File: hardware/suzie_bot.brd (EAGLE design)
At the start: 98.7 x 71.1 mm, 20 parts, among them IC1 LT1529CT33, IC2 L9637DDIP-ADAPTED, Y1 1.8432, Y2 6.0

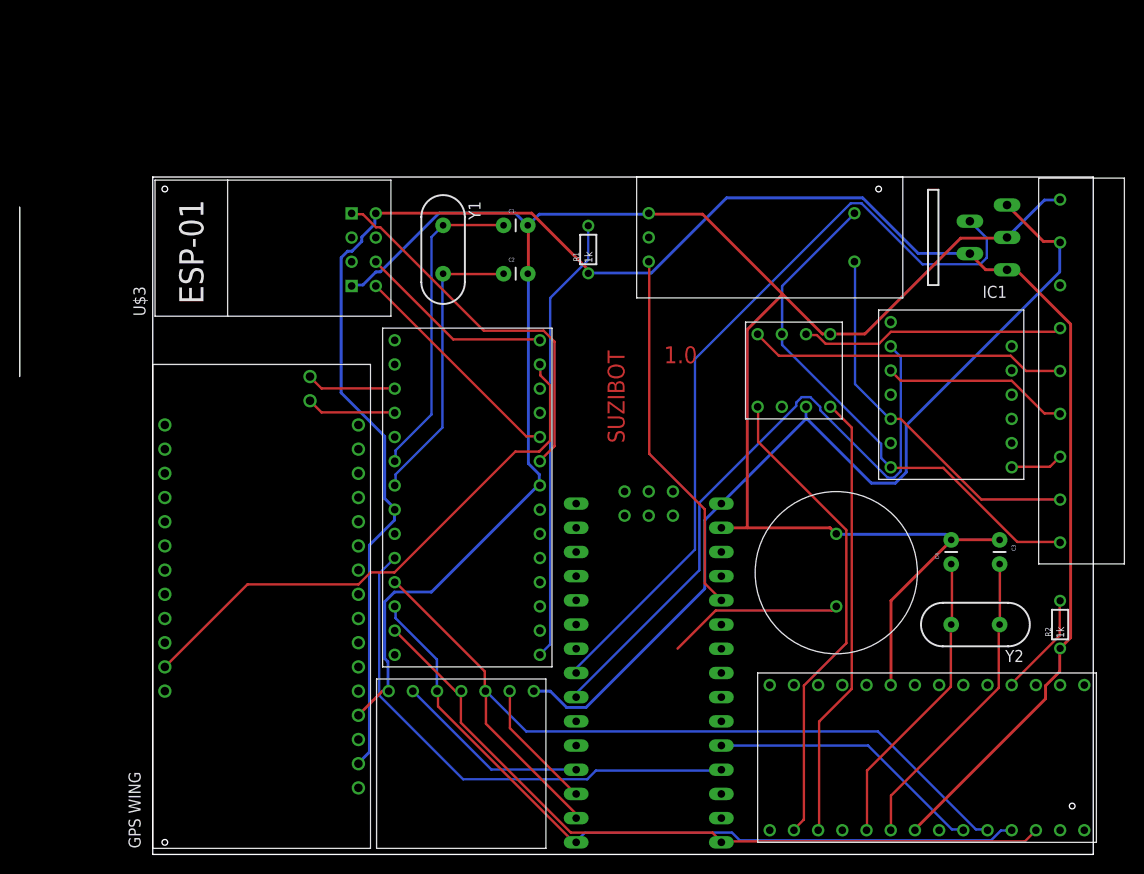
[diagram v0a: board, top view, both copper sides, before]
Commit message: Totally working. IT WAS VOLTAGE LEVELS AND CRYSTAL CAPACITANCE PROBLEMS ALL ALONG.
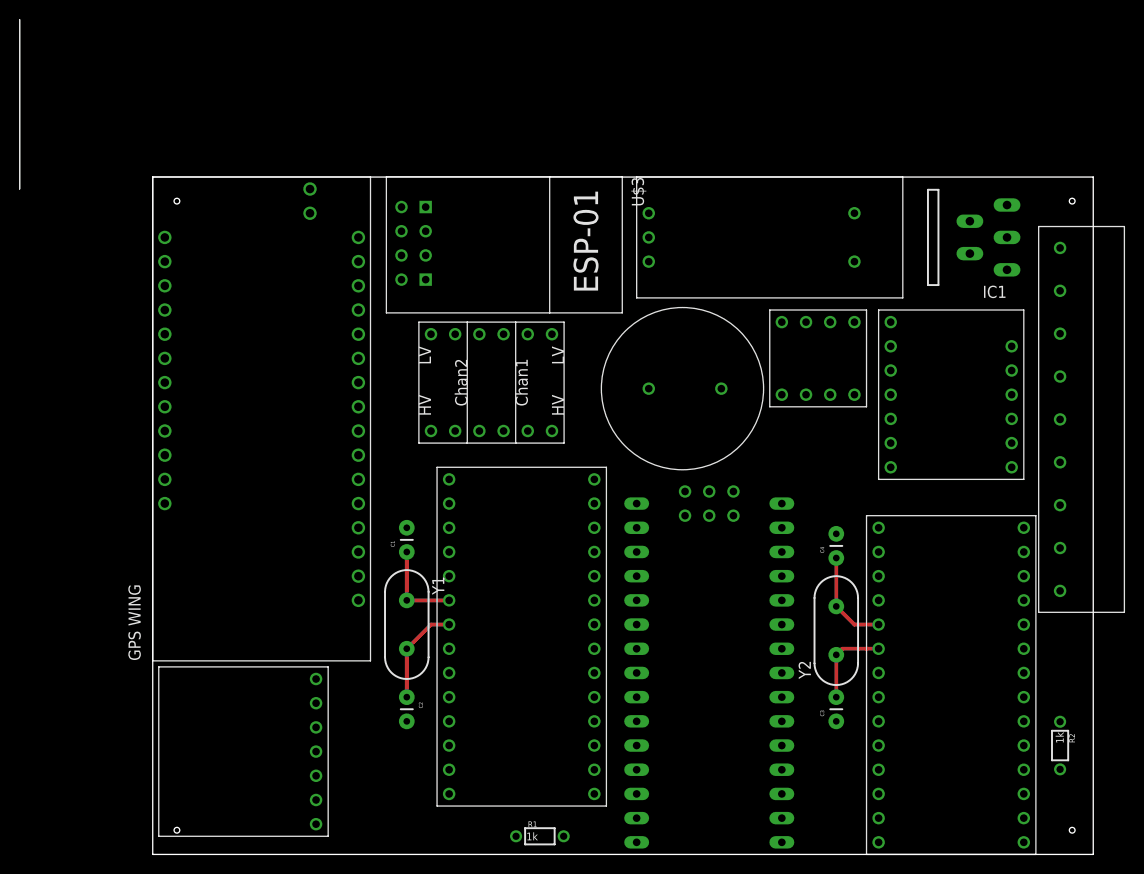
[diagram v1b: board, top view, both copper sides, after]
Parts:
- added U$6: LOGIC_LEVEL_CONVERTER, SparkFun-Boards:LOGIC_LEVEL_CONVERTER
- Y1: value 1.8432 -> 14.7456
- moved R1 61.8 mm to (40.6, 1.91), turned to 0 degrees
- moved C2 45.6 mm to (26.7, 16.5), turned to 270 degrees
- moved Y1 39.6 mm to (26.7, 24.1)
- moved C1 35.8 mm to (26.7, 31.8), turned to 90 degrees
- moved U$11 26.6 mm to (54.6, 48.9), turned to 180 degrees
- moved C3 25.6 mm to (71.8, 14.0), turned to 90 degrees
- moved U$5 19.7 mm to (16.5, 74.9)
- moved U$3 19.1 mm to (34.3, 64.1), turned to 270 degrees
- moved U$7 17.7 mm to (81.3, 24.1), turned to 0 degrees
- moved U$2 15.7 mm to (36.2, 29.2)
- moved Y2 14.6 mm to (71.8, 23.5), turned to 90 degrees
- moved U$9 13.3 mm to (17.1, 13.3), turned to 90 degrees
- moved R2 12.7 mm to (95.2, 11.4), turned to 270 degrees
- moved C4 12.1 mm to (71.8, 31.1)
- moved U$1 6.35 mm to (55.9, 27.9)
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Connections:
- new net N$22: U$2.P$23, U$6.P$8
- new net N$23: U$2.P$24, U$6.P$7
- new net N$24: U$2.P$3, U$6.P$12
- new net N$25: U$2.P$4, U$6.P$11
- net 3V3: now also U$6.P$3
- net 5V: now also U$6.P$10
- net GND: now also U$6.P$4, U$6.P$9
- net N$14: now also U$6.P$2; no longer U$2.P$4
- net N$17: now also U$6.P$1; no longer U$2.P$3
- net N$5: now also U$6.P$6; no longer U$2.P$24
- net N$8: now also U$6.P$5; no longer U$2.P$23
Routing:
- net GND: track 226.5 -> 0.00 mm
- net 3V3: track 208.0 -> 0.00 mm
- net 5V: track 99.2 -> 0.00 mm
- net MOSI: track 91.5 -> 0.00 mm
- net N$34: track 83.0 -> 0.00 mm
- net MISO: track 79.8 -> 0.00 mm
- net SCLK: track 79.1 -> 0.00 mm
- net N$29: track 69.2 -> 0.00 mm
- net N$2: track 58.8 -> 0.00 mm
- net N$7: track 55.6 -> 0.00 mm
- net N$33: track 55.1 -> 0.00 mm
- net N$15: track 50.6 -> 0.00 mm
- net N$18: track 47.1 -> 0.00 mm
- net N$19: track 46.9 -> 0.00 mm
- net N$8: track 40.1 -> 0.00 mm
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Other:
- board text removed: "1.0"
- board text removed: "SUZIBOT"

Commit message: Basic working features.
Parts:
- removed U$8: 9-PIN-TERMINATION-BLOCK, randomjunk:9-PIN-HEADER-BLOCK
- added 12V-IN/GND, 12V-OUT/ON, GND/5V, K/L: 2-PIN-TERMINAL, randomjunk:2-PIN-TERMINAL
- U$3: value ESP01 -> (none)
- U$7: value SC16IS750IPWDIP-ADAPTER -> SC16IS750IPWDIP-24; device nxp-semiconductors:TSSOP-28-ADAPTED -> nxp-semiconductors:TSSOP-24-ADAPTED
- U$9: value LEVEL-CONVERTING-MICROSD -> (none)
- moved IC2 16.1 mm to (86.4, 58.4)
- moved U$7 10.2 mm to (81.9, 14.0)
- moved U$11 10.2 mm to (64.8, 48.9)
- moved IC1 9.09 mm to (85.1, 73.0), turned to 0 degrees
- moved C2 6.98 mm to (26.7, 23.5)
- moved Y1 6.35 mm to (26.7, 30.5)
- moved U$4 5.85 mm to (81.3, 42.5)
- moved C1 5.72 mm to (26.7, 37.5)
- moved C4 4.26 mm to (69.8, 27.3)
- moved C3 3.70 mm to (69.8, 10.8)
- moved Y2 3.70 mm to (69.8, 20.3)
- moved U$6 3.18 mm to (24.8, 55.9)
- moved R2 2.84 mm to (92.7, 10.2)
- moved U$1 0.64 mm to (55.2, 27.9)
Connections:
- removed net N$10: U$10.GND, U$4.GND3, U$8.P$2
- removed net N$11 (its old number): U$4.ON, U$8.P$4
- removed net N$12: IC2.K, U$8.P$6
- removed net N$13: IC2.LI, U$8.P$5
- removed net N$7: IC2.VS, U$10.VCC, U$4.VIN1, U$8.P$1
- removed net N$9: U$4.VOUT1, U$8.P$3
- new net 12V-IN: 12V-IN/GND.P$1, U$4.VIN1
- new net 12V-OUT: 12V-OUT/ON.P$1, IC2.VS, U$10.VCC, U$4.VOUT1
- new net EXT-GND: 12V-IN/GND.P$2, U$10.GND, U$4.GND3
- new net K: IC2.K, K/L.P$1
- new net L: IC2.LI, K/L.P$2
- new net POWERON: 12V-OUT/ON.P$2, U$4.ON
- net 5V: now also GND/5V.P$2; no longer U$8.P$8
- net GND: now also GND/5V.P$1, U$7.P$19; no longer U$7.P$23, U$8.P$9
- net N$16: now also U$7.P$14; no longer U$7.P$18
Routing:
- net GND: track 0.00 -> 272.9 mm
- net 3V3: track 0.00 -> 229.5 mm
- net 5V: track 0.00 -> 154.8 mm, vias 0 -> 1
- net MOSI: track 0.00 -> 71.5 mm
- net MISO: track 0.00 -> 66.6 mm
- net N$34: track 0.00 -> 65.2 mm
- net SCLK: track 0.00 -> 61.2 mm
- net 12V-OUT: track 0.00 -> 47.8 mm
- net EXT-GND: track 0.00 -> 43.6 mm
- net N$11: track 0.00 -> 43.0 mm
- net N$30: track 0.00 -> 41.1 mm
- net N$19: track 0.00 -> 39.2 mm
- net N$33: track 0.00 -> 37.5 mm
- net N$6: track 0.00 -> 36.0 mm
- net N$4: track 0.00 -> 35.4 mm
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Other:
- board text added: "1.0"
- board text added: "12VIN"
- board text added: "5V"
- board text added: "GND"
- board text added: "K"
- board text added: "L"
- board text added: "ON"
- board text added: "SUZIBOT"
- board text added: "VOUT"

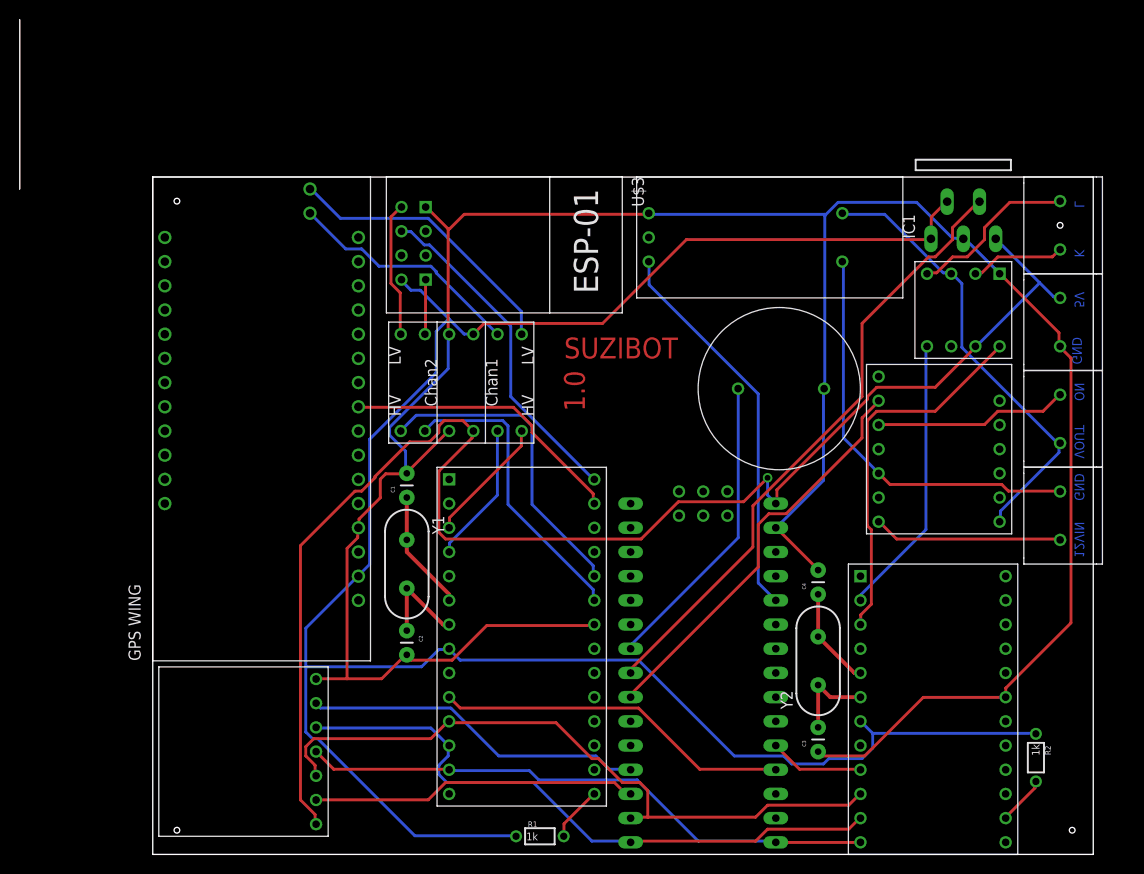
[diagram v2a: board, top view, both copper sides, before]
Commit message: Adding a ground plane at @nbanerje's suggestion.  Thanks @nbanerje!
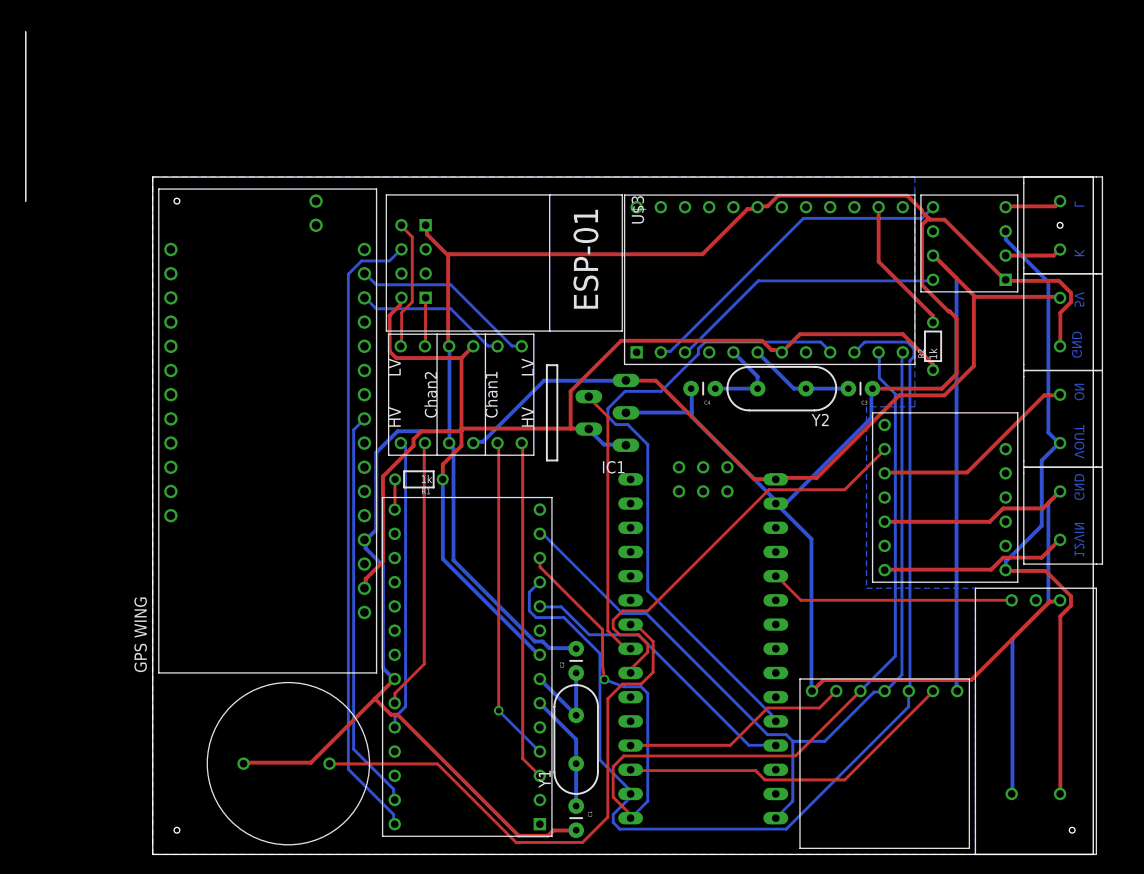
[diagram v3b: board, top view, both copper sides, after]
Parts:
- moved U$11 63.3 mm to (15.2, 9.53), turned to 0 degrees
- moved U$9 57.3 mm to (74.3, 17.1), turned to 180 degrees
- moved U$10 55.7 mm to (92.7, 26.7), turned to 180 degrees
- moved IC1 51.3 mm to (41.3, 46.4), turned to 90 degrees
- moved U$7 49.0 mm to (66.0, 60.3), turned to 90 degrees
- moved R2 44.5 mm to (81.9, 53.3), turned to 90 degrees
- moved R1 39.6 mm to (27.9, 39.4), turned to 180 degrees
- moved C3 38.5 mm to (75.6, 48.9), turned to 180 degrees
- moved C1 36.9 mm to (44.5, 5.08), turned to 270 degrees
- moved Y2 28.8 mm to (66.0, 48.9), turned to 180 degrees
- moved Y1 25.6 mm to (44.5, 12.1), turned to 90 degrees
- moved C4 24.1 mm to (59.1, 48.9), turned to 180 degrees
- moved C2 18.3 mm to (44.5, 19.1), turned to 90 degrees
- moved U$2 15.9 mm to (35.6, 13.3), turned to 180 degrees
- moved U$4 5.12 mm to (81.9, 37.5)
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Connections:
- net 12V-IN renamed N$7
- net EXT-GND renamed EXTGND
- net N$14: now also U$5.TX-2; no longer U$5.TX
- net N$17: now also U$5.RX-2; no longer U$5.RX
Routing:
- net 3V3: track 229.5 -> 140.7 mm
- net GND: track 272.9 -> 331.7 mm
- net CS-KLINE: track 9.93 -> 67.9 mm
- net MOSI: track 71.5 -> 114.0 mm
- net MISO: track 66.6 -> 107.5 mm, vias 0 -> 1
- net N$34: track 65.2 -> 28.6 mm
- net SCLK: track 61.2 -> 92.8 mm
- net N$4: track 35.4 -> 66.4 mm
- net N$36: track 32.0 -> 58.4 mm
- net N$24: track 13.3 -> 35.8 mm
- net 12V-OUT: track 47.8 -> 69.6 mm
- net 5V: track 154.8 -> 133.9 mm, vias 1 -> 0
- net N$25: track 14.8 -> 34.3 mm, vias 0 -> 1
- net N$30: track 41.1 -> 25.8 mm
- net N$2: track 29.9 -> 42.3 mm
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- added copper zone on layer 16, net GND
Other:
- board text removed: "1.0"
- board text removed: "SUZIBOT"

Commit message: Minor changes to improve positioning.
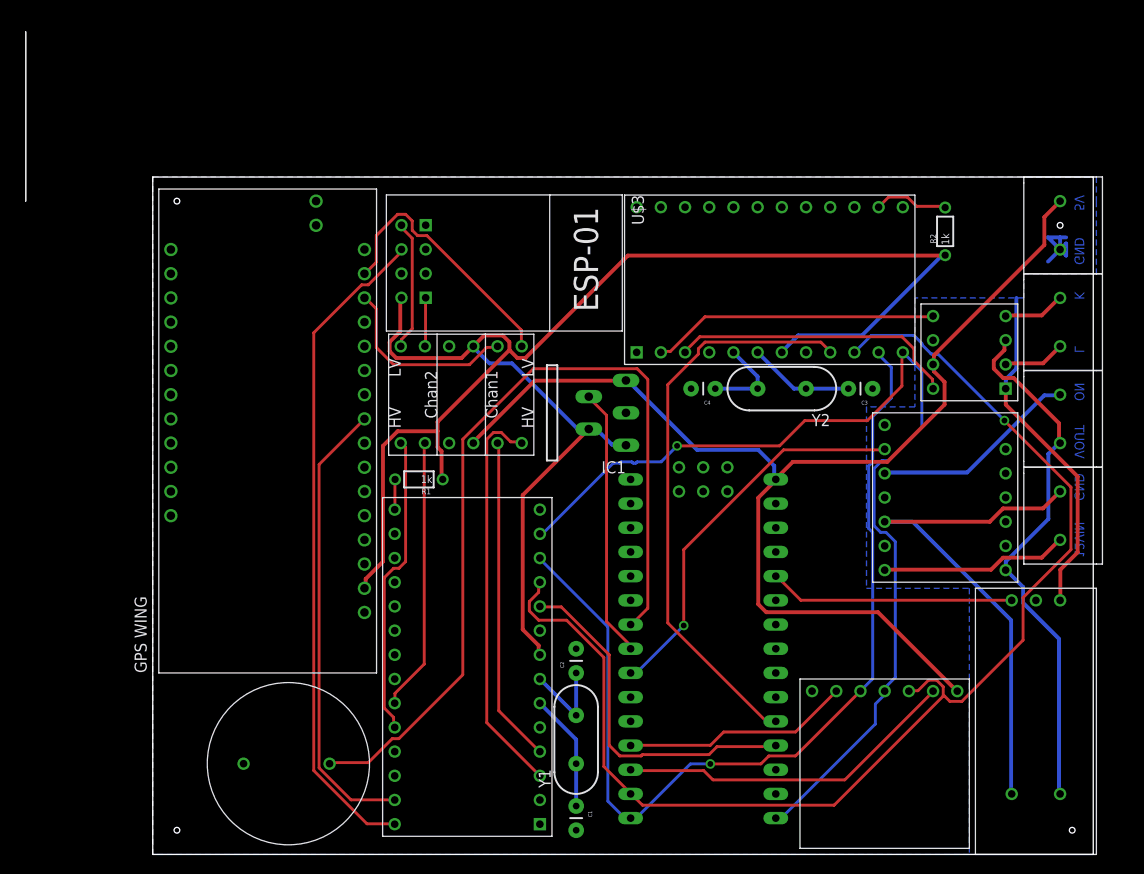
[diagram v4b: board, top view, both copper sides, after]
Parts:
- moved R2 12.1 mm to (83.2, 65.4)
- moved IC2 11.4 mm to (87.0, 51.4)
- moved GND/5V 10.2 mm to (95.2, 66.0)
- moved K/L 10.2 mm to (95.2, 55.9)
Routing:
- net GND: track 331.7 -> 46.0 mm
- net 3V3: track 140.7 -> 180.1 mm
- net N$36: track 58.4 -> 92.1 mm
- net MOSI: track 114.0 -> 131.8 mm, vias 0 -> 1
- net SCLK: track 92.8 -> 107.2 mm, vias 0 -> 1
- net 12V-OUT: track 69.6 -> 56.5 mm
- net MISO: track 107.5 -> 99.1 mm
- net N$17: track 19.7 -> 28.0 mm
- net CS-KLINE: track 67.9 -> 60.4 mm
- net 5V: track 133.9 -> 126.4 mm
- net N$16: track 14.5 -> 7.92 mm
- net N$33: track 30.8 -> 37.3 mm
- net N$24: track 35.8 -> 42.1 mm
- net N$2: track 42.3 -> 47.9 mm
- net N$15: track 34.9 -> 30.2 mm
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
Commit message: Some routing alterations; fixing SD card package sizing.
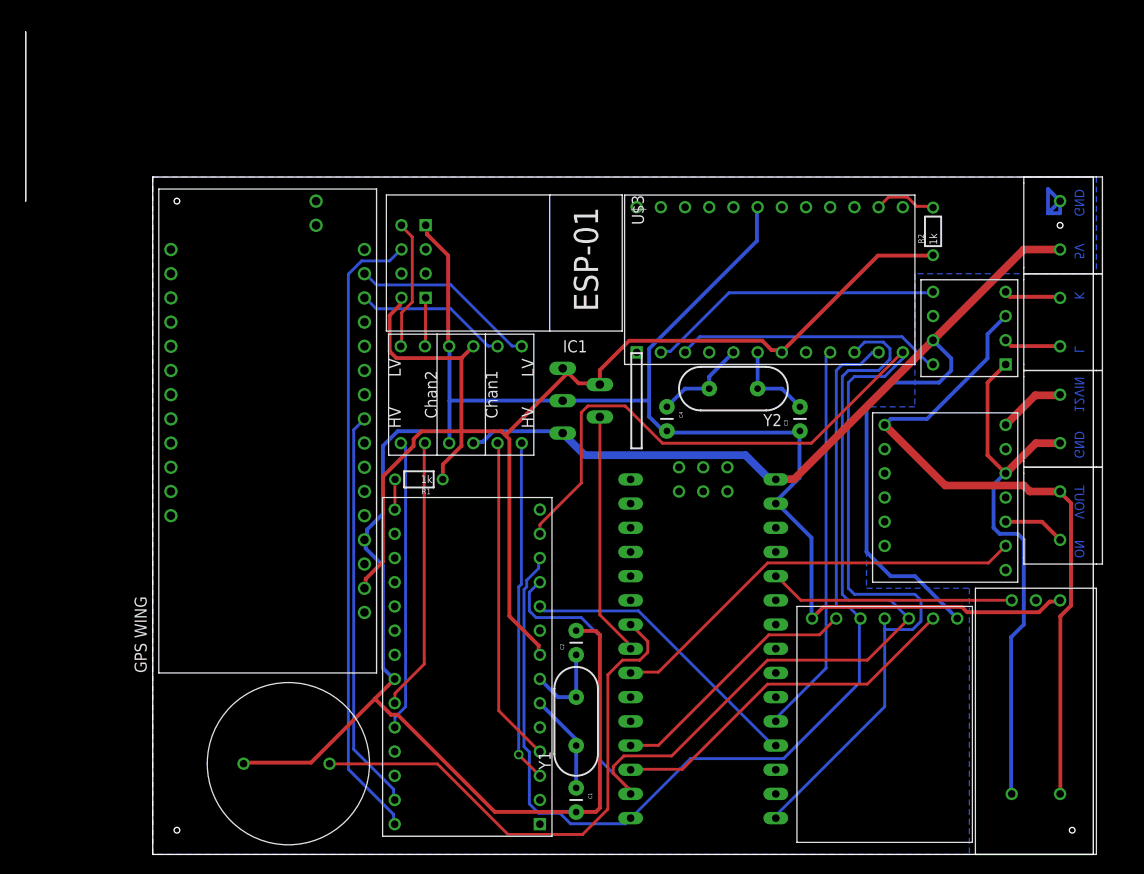
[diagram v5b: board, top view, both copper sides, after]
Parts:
- moved IC1 10.2 mm to (51.4, 47.6), turned to 270 degrees
- moved C3 8.82 mm to (67.9, 44.5), turned to 90 degrees
- moved U$9 7.62 mm to (74.3, 24.8)
- moved C4 5.43 mm to (54.0, 47.0), turned to 270 degrees
- moved Y2 5.08 mm to (61.0, 48.9)
- moved IC2 2.54 mm to (87.0, 54.0)
- moved U$4 2.54 mm to (84.5, 37.5), turned to 0 degrees
- moved Y1 1.91 mm to (44.5, 14.0)
- moved C1 1.91 mm to (44.5, 6.99)
- moved C2 1.90 mm to (44.5, 21.0)
- moved R2 1.27 mm to (81.9, 65.4)
- renumbered 12V-IN/GND to ON/12V-OUT, 12V-OUT/ON to GND/12V-IN, GND/5V to 5V/GND
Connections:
- net 12V-OUT: now also ON/12V-OUT.P$2; no longer GND/12V-IN.P$1
- net 5V: now also 5V/GND.P$1; no longer 5V/GND.P$2
- net EXTGND: now also GND/12V-IN.P$1, IC2.GND; no longer ON/12V-OUT.P$2
- net GND: now also 5V/GND.P$2; no longer 5V/GND.P$1, IC2.GND
- net N$7: now also GND/12V-IN.P$2; no longer ON/12V-OUT.P$1
- net POWERON: now also ON/12V-OUT.P$1; no longer GND/12V-IN.P$2
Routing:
- net GND: track 46.0 -> 250.1 mm
- net 3V3: track 180.1 -> 139.0 mm
- net N$36: track 92.1 -> 56.3 mm
- net CS-KLINE: track 60.4 -> 41.2 mm
- net MOSI: track 131.8 -> 113.3 mm, vias 1 -> 0
- net 12V-OUT: track 56.5 -> 72.9 mm, vias 0 -> 1
- net SCLK: track 107.2 -> 123.4 mm, vias 1 -> 0
- net POWERON: track 21.9 -> 6.53 mm
- net N$7: track 19.7 -> 7.06 mm
- net 5V: track 126.4 -> 116.8 mm, vias 0 -> 1
- net MISO: track 99.1 -> 108.3 mm, vias 1 -> 0
- net N$17: track 28.0 -> 19.7 mm
- net N$33: track 37.3 -> 30.8 mm
- net N$24: track 42.1 -> 36.0 mm, vias 0 -> 1
- net N$2: track 47.9 -> 42.3 mm
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
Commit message: Routing a bunch of wires further from the pins.
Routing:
- net N$4: track 66.4 -> 78.5 mm
- net N$2: track 42.3 -> 49.3 mm
- net MISO: track 108.3 -> 112.8 mm
- net 5V: track 116.8 -> 120.9 mm, vias 1 -> 0
- net N$24: track 36.0 -> 39.4 mm
- net N$19: track 28.0 -> 31.1 mm
- net N$17: track 19.7 -> 22.3 mm
- net N$23: track 30.6 -> 32.5 mm
- net N$14: track 16.1 -> 17.6 mm
- net 12V-OUT: vias 1 -> 0
